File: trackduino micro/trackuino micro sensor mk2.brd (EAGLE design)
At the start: 43.3 x 19.1 mm, 42 parts, among them IC2 74AHC1G125DBV, SW1 SPST_TACT-KMR2, U1 ATMEGA168MLF, Y1 16MHZ

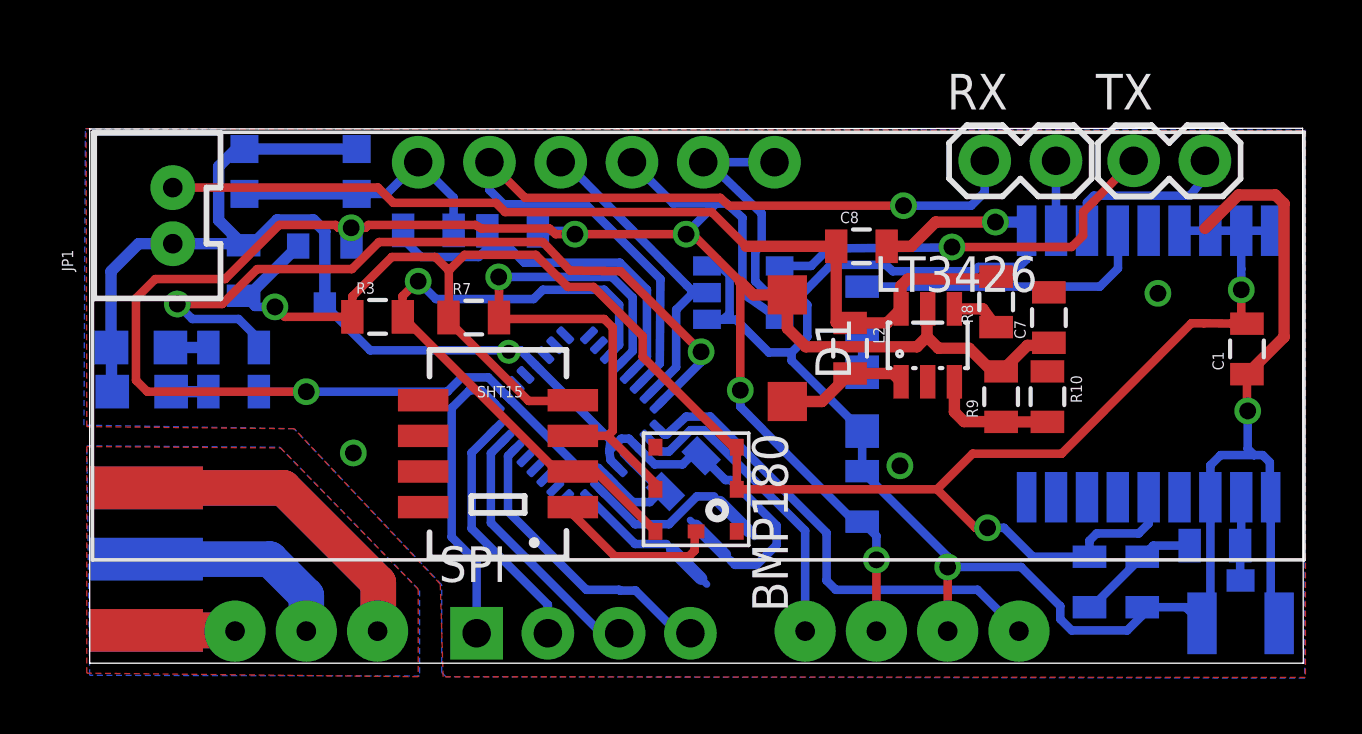
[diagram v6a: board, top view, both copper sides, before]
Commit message: replaced inductor
the 0805 inductor was getting way too hot due to being run well beyond
saturation. replaced with a 1812 inductor
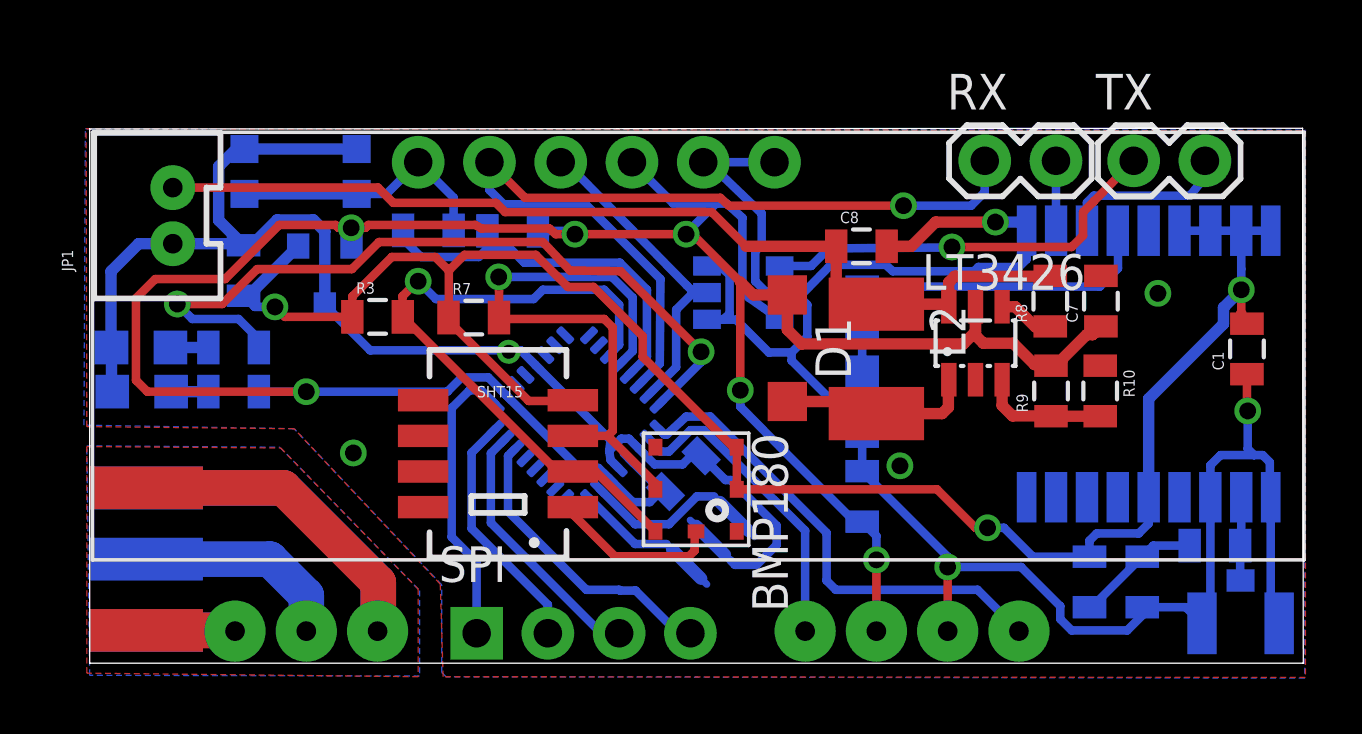
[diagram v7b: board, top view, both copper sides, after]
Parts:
- L2: device SparkFun-Passives:0805 -> resistor:L1812
- moved C7 1.94 mm to (87.4, 70.4)
- moved R8 1.93 mm to (85.6, 70.4)
- moved R10 1.89 mm to (87.4, 67.2)
- moved R9 1.79 mm to (85.6, 67.2)
- moved LT3426 1.70 mm to (83.0, 68.9)
- moved L2 1.01 mm to (79.4, 68.4)
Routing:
- net GND: track 166.5 -> 156.5 mm
- net 3V: track 72.1 -> 67.3 mm
- net VCC: track 93.1 -> 96.0 mm
- net N$9: track 4.59 -> 7.00 mm

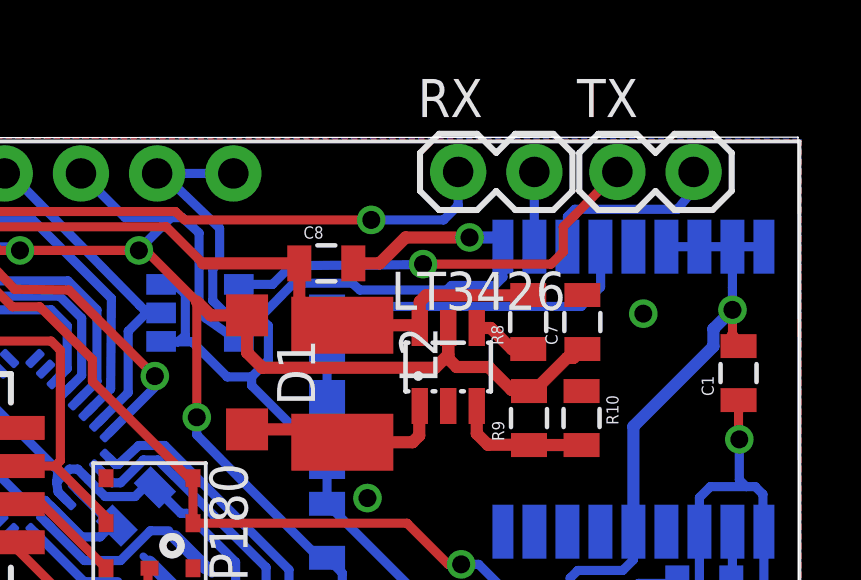
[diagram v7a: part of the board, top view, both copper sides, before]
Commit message: added output cap
added a larger value output cap
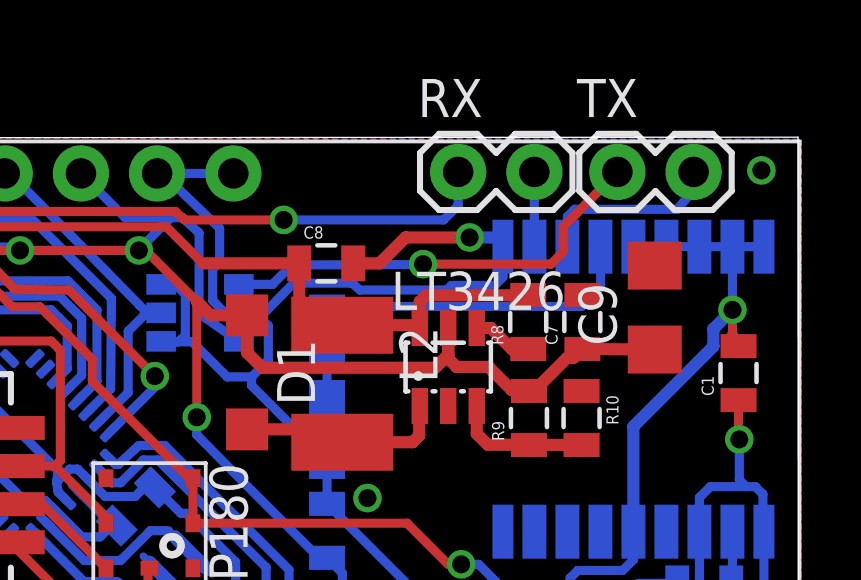
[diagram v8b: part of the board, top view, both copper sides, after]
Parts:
- added C9: 100uf, resistor:C1206
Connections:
- net GND: now also C9.2
- net VCC: now also C9.1
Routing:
- net VCC: track 96.0 -> 98.4 mm
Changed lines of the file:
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@@
 <element name="C7" library="SparkFun-Capacitors" package="0805" value="22uf" x="87.4268" y="70.4088" rot="R90"/>
 <element name="C8" library="SparkFun-Capacitors" package="0805" value="10uf" x="78.8924" y="72.3646"/>
+<element name="C9" library="resistor" package="C1206" value="100uf" x="89.8398" y="70.8914" rot="R90"/>
 </elements>
 <signals>
@@
 <wire x1="83.6676" y1="73.2282" x2="84.5732" y2="73.2282" width="0.4064" layer="16"/>
 <wire x1="84.5732" y1="73.2282" x2="84.7794" y2="72.9204" width="0.4064" layer="16"/>
-<via x="89.4588" y="70.6882" extent="1-16" drill="0.6" shape="square"/>
+<via x="93.3958" y="75.4634" extent="1-16" drill="0.6" shape="square"/>
 <via x="60.7822" y="64.9986" extent="1-16" drill="0.6" shape="square"/>
 <via x="66.3194" y="68.6054" extent="1-16" drill="0.5"/>
+<contactref element="C9" pad="2"/>
 <wire x1="56.5658" y1="58.6486" x2="56.5912" y2="58.674" width="0" layer="19" extent="1-1"/>
 <wire x1="60.7822" y1="64.9986" x2="58.293" y2="63.754" width="0" layer="19" extent="1-1"/>
@@
 <wire x1="76.2508" y1="69.3928" x2="76.7588" y2="68.8848" width="0.4064" layer="1"/>
 <wire x1="76.7588" y1="68.8848" x2="82.5246" y2="68.8848" width="0.4064" layer="1"/>
+<contactref element="C9" pad="1"/>
+<wire x1="87.4268" y1="69.5088" x2="87.5906" y2="69.5088" width="0.4064" layer="1"/>
+<wire x1="87.5906" y1="69.5088" x2="89.8398" y2="69.4914" width="0.4064" layer="1"/>
 </signal>
 <signal name="D3">
@@
 <wire x1="83.2866" y1="75.4126" x2="83.2866" y2="74.295" width="0.3048" layer="16"/>
 <wire x1="83.2866" y1="74.295" x2="82.804" y2="73.8124" width="0.3048" layer="16"/>
-<wire x1="82.804" y1="73.8124" x2="80.391" y2="73.8124" width="0.3048" layer="16"/>
-<via x="80.391" y="73.8124" extent="1-16" drill="0.6" shape="square"/>
-<wire x1="80.391" y1="73.8124" x2="74.168" y2="73.8124" width="0.3048" layer="1"/>
+<wire x1="82.804" y1="73.8124" x2="77.47" y2="73.8124" width="0.3048" layer="16"/>
+<via x="77.47" y="73.8124" extent="1-16" drill="0.6" shape="square"/>
+<wire x1="77.47" y1="73.8124" x2="74.168" y2="73.8124" width="0.3048" layer="1"/>
 <wire x1="74.168" y1="73.8124" x2="73.8632" y2="74.0918" width="0.3048" layer="1"/>
 <wire x1="73.8632" y1="74.0918" x2="66.9036" y2="74.0918" width="0.3048" layer="1"/>
@@
 <contactref element="TX" pad="1"/>
 <wire x1="75.976" y1="71.6636" x2="77.0992" y2="71.6636" width="0.3048" layer="16"/>
-<wire x1="77.0992" y1="71.6636" x2="77.724" y2="72.2884" width="0.3048" layer="16"/>
-<wire x1="77.724" y1="72.2884" x2="82.103" y2="72.324" width="0.3048" layer="16"/>
+<wire x1="77.0992" y1="71.6636" x2="77.7494" y2="72.3138" width="0.3048" layer="16"/>
+<wire x1="77.7494" y1="72.3138" x2="82.103" y2="72.324" width="0.3048" layer="16"/>
 <wire x1="82.103" y1="72.324" x2="82.1182" y2="72.3392" width="0.3048" layer="16"/>
 <via x="82.1182" y="72.3392" extent="1-16" drill="0.6" shape="square"/>
